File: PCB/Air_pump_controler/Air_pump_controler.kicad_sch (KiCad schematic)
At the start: 28 parts, among them J1 Conn_01x03_Pin, J2 USB IN, J4 Motor_conn, Q1 AP30N03DF, U1 CH32V003F4U6

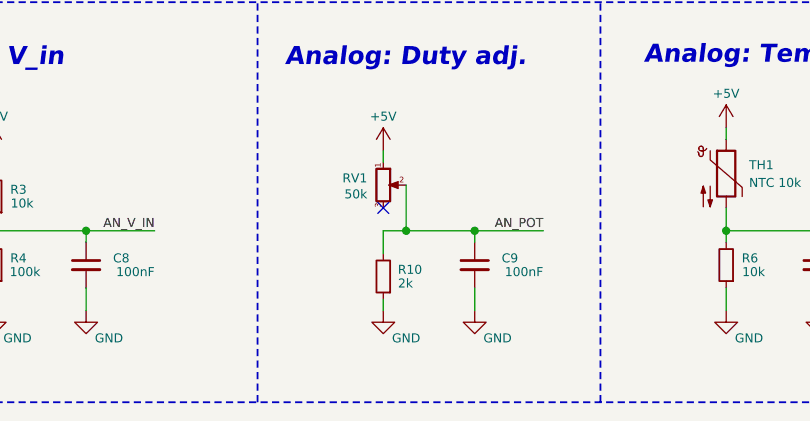
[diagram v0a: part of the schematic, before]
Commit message: Update
input voltage compensation for duty cycle
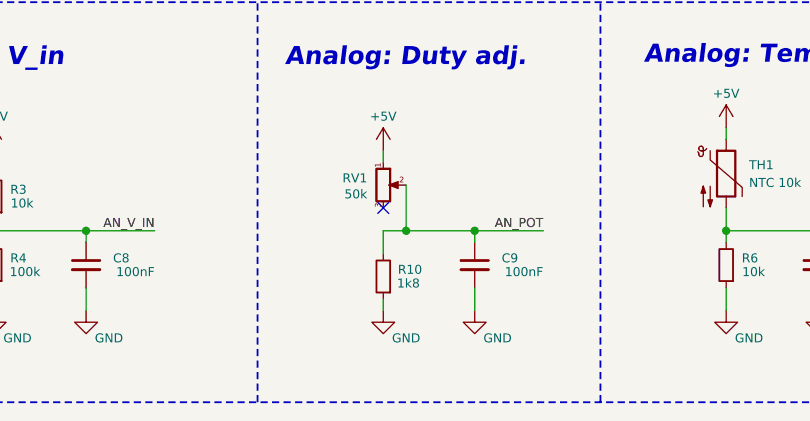
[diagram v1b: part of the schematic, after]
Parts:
- R10: value 2k -> 1k8
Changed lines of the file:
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@@
 			)
 		)
-		(property "Value" "2k"
-			(at 71.882 112.522 0)
+		(property "Value" "1k8"
+			(at 72.644 112.522 0)
 			(effects
 				(font

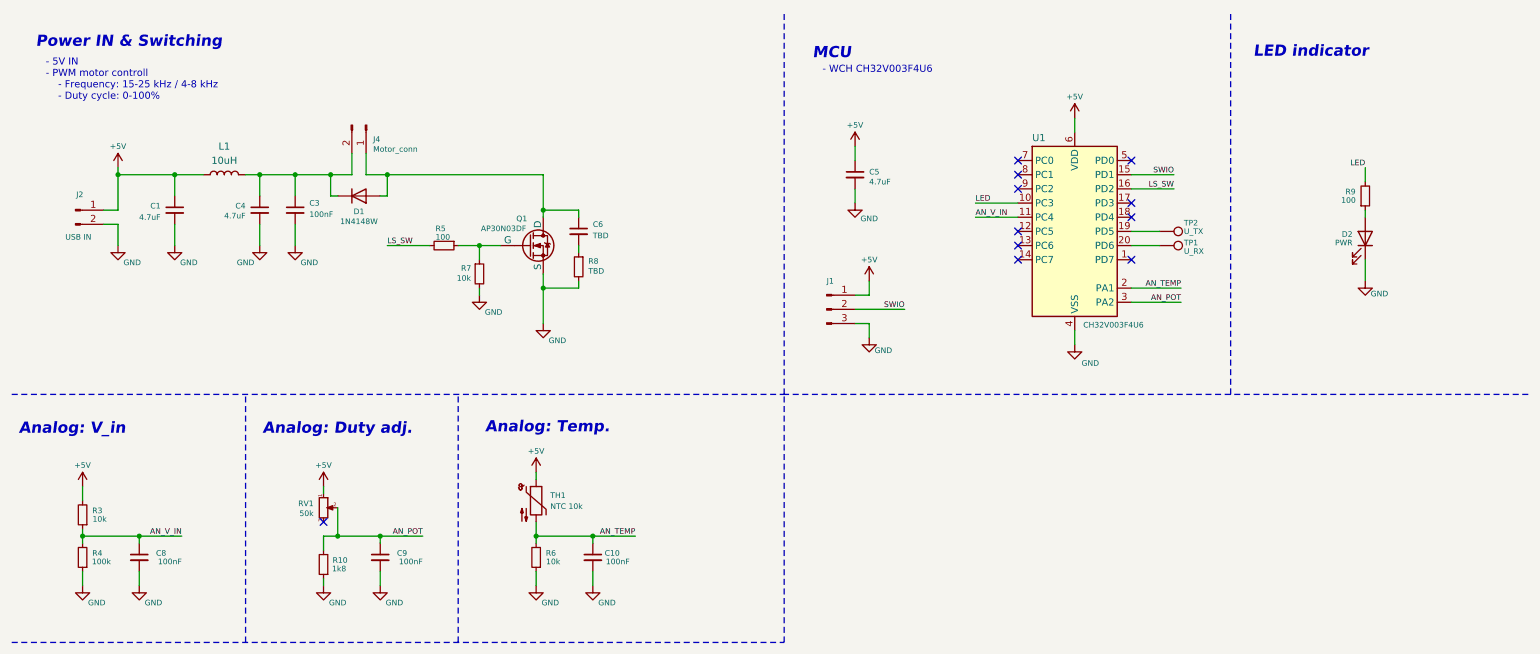
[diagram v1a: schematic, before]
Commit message: Update
changed potenciometer voltage divider, added filter cap
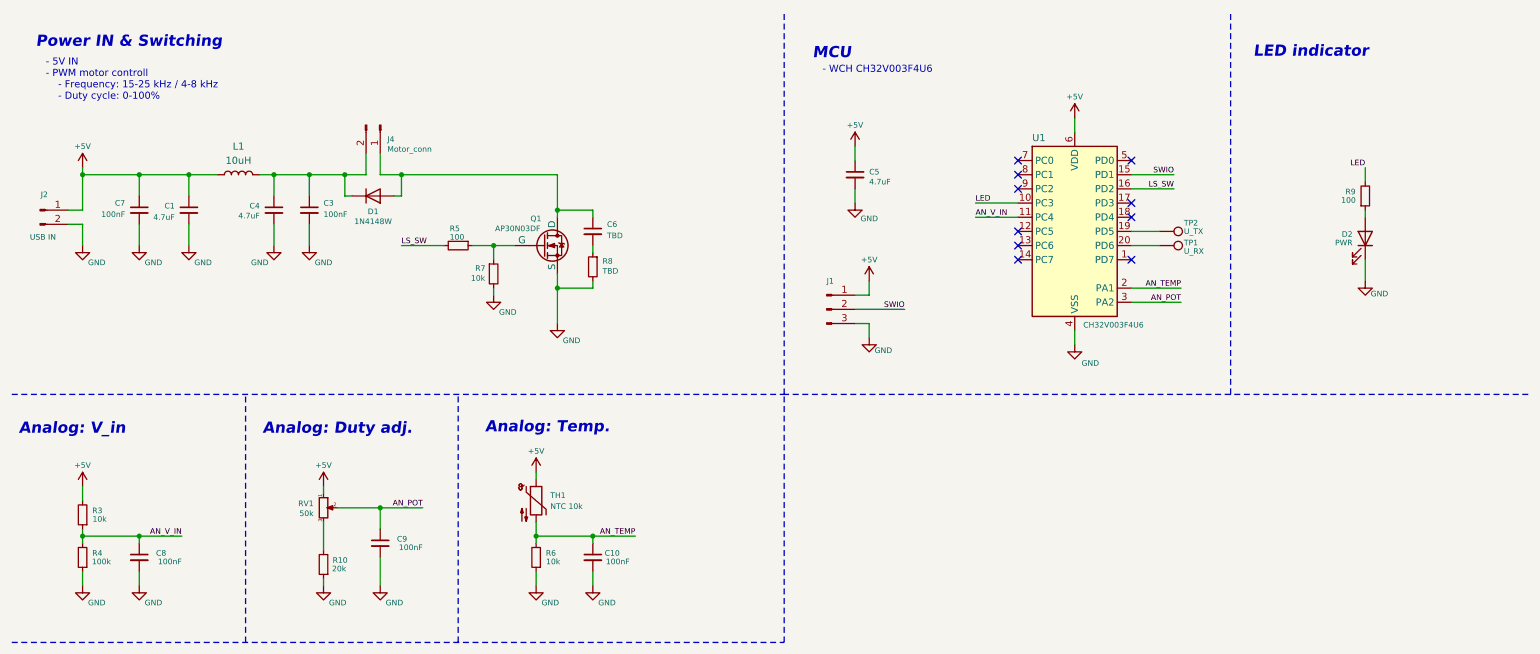
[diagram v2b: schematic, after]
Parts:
- added C7: 100nF, Capacitor_SMD:C_0603_1608Metric, symbol Device:C_Small
- R10: value 1k8 -> 20k
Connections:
- net +5V: now also C7.1
- net AN_POT: no longer R10.2
- net GND: now also C7.2
- net at RV1.3: now also R10.2
- no-connect marks 11 -> 10
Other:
- moved on the sheet: C1, C3, C4, C6, C9, D1, J2, J4, L1, Q1, R5, R7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

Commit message: Update
added filter cap on input
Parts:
- removed C7: 100nF, Capacitor_SMD:C_0603_1608Metric, symbol Device:C_Small
- added C11, C12: 10nF, Capacitor_SMD:C_0402_1005Metric, symbol Device:C_Small
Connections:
- net +5V: now also C11.1, C12.1
- net GND: now also C11.2, C12.2
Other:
- moved on the sheet: C1, C3, C4, C6, D1, J4, L1, Q1, R5, R7, R8

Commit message: Update
added filter cap on input
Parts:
- added C13: 10nF, Capacitor_SMD:C_0402_1005Metric, symbol Device:C_Small
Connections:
- net +5V: now also C13.1
- net GND: now also C13.2
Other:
- moved on the sheet: C5
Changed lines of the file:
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@@
 	)
 	(junction
+		(at 167.64 38.1)
+		(diameter 0)
+		(color 0 0 0 0)
+	)
+	(junction
 		(at 74.93 41.91)
 		(diameter 0)
@@
 	(wire
 		(pts
-			(xy 163.83 44.45) (xy 163.83 46.99)
+			(xy 167.64 44.45) (xy 167.64 46.99)
 		)
 		(stroke
@@
 	(wire
 		(pts
+			(xy 162.56 39.37) (xy 162.56 38.1)
+		)
+		(stroke
+			(width 0)
+			(type default)
+		)
+	)
+	(wire
+		(pts
 			(xy 102.87 45.72) (xy 104.14 45.72)
 		)
@@
 	(wire
 		(pts
+			(xy 162.56 44.45) (xy 162.56 46.99)
+		)
+		(stroke
+			(width 0)
+			(type default)
+		)
+	)
+	(wire
+		(pts
 			(xy 93.98 45.72) (xy 93.98 41.91)
 		)
@@
 	(wire
 		(pts
-			(xy 163.83 36.83) (xy 163.83 39.37)
+			(xy 167.64 36.83) (xy 167.64 38.1)
 		)
 		(stroke
@@
 	(wire
 		(pts
+			(xy 162.56 38.1) (xy 167.64 38.1)
+		)
+		(stroke
+			(width 0)
+			(type default)
+		)
+	)
+	(wire
+		(pts
 			(xy 35.56 50.8) (xy 35.56 54.61)
 		)
@@
 	(wire
 		(pts
+			(xy 167.64 38.1) (xy 167.64 39.37)
+		)
+		(stroke
+			(width 0)
+			(type default)
+		)
+	)
+	(wire
+		(pts
 			(xy 35.56 113.03) (xy 35.56 115.57)
 		)
@@
 	)
 	(symbol
+		(lib_id "Device:C_Small")
+		(at 162.56 41.91 0)
+		(mirror y)
+		(unit 1)
+		(exclude_from_sim no)
+		(in_bom yes)
+		(on_board yes)
+		(dnp no)
+		(property "Reference" "C13"
+			(at 160.02 41.402 0)
+			(effects
+				(font
+					(size 1 1)
+				)
+				(justify left)
+			)
+		)
+		(property "Value" "10nF"
+			(at 160.02 43.1863 0)
+			(effects
+				(font
+					(size 1 1)
+				)
+				(justify left)
+			)
+		)
+		(property "Footprint" "Capacitor_SMD:C_0402_1005Metric"
+			(at 162.56 41.91 0)
+			(effects
+				(font
+					(size 1.27 1.27)
+				)
+				(hide yes)
+			)
+		)
+		(property "Datasheet" "~"
+			(at 162.56 41.91 0)
+			(effects
+				(font
+					(size 1.27 1.27)
+				)
+				(hide yes)
+			)
+		)
+		(property "Description" "Unpolarized capacitor, small symbol"
+			(at 162.56 41.91 0)
+			(effects
+				(font
+					(size 1.27 1.27)
+				)
+				(hide yes)
+			)
+		)
+		(pin "1"
+		)
+		(pin "2"
+		)
+		(instances
+			(project "Air_pump_controler"
+				(path "/3c68f82e-901f-404a-869f-4b45aa33f8e4"
+					(reference "C13")
+					(unit 1)
+				)
+			)
+		)
+	)
+	(symbol
 		(lib_id "power:GND")
-		(at 163.83 46.99 0)
+		(at 167.64 46.99 0)
 		(unit 1)
 		(exclude_from_sim no)
@@
 		(dnp no)
 		(property "Reference" "#PWR04"
-			(at 163.83 53.34 0)
+			(at 167.64 53.34 0)
 			(effects
 				(font
@@
 		)
 		(property "Value" "GND"
-			(at 166.37 49.784 0)
+			(at 170.18 49.784 0)
 			(effects
 				(font
@@
 		)
 		(property "Footprint" ""
-			(at 163.83 46.99 0)
+			(at 167.64 46.99 0)
 			(effects
 				(font
@@
 		)
 		(property "Datasheet" ""
-			(at 163.83 46.99 0)
+			(at 167.64 46.99 0)
 			(effects
 				(font
@@
 		)
 		(property "Description" "Power symbol creates a global label with name \"GND\" , ground"
-			(at 163.83 46.99 0)
+			(at 167.64 46.99 0)
 			(effects
 				(font
@@
 	(symbol
 		(lib_id "power:GND")
+		(at 162.56 46.99 0)
+		(mirror y)
+		(unit 1)
+		(exclude_from_sim no)
+		(in_bom yes)
+		(on_board yes)
+		(dnp no)
+		(property "Reference" "#PWR025"
+			(at 162.56 53.34 0)
+			(effects
+				(font
+					(size 1.27 1.27)
+				)
+				(hide yes)
+			)
+		)
+		(property "Value" "GND"
+			(at 160.02 50.038 0)
+			(effects
+				(font
+					(size 1 1)
+				)
+			)
+		)
+		(property "Footprint" ""
+			(at 162.56 46.99 0)
+			(effects
+				(font
+					(size 1.27 1.27)
+				)
+				(hide yes)
+			)
+		)
+		(property "Datasheet" ""
+			(at 162.56 46.99 0)
+			(effects
+				(font
+					(size 1.27 1.27)
+				)
+				(hide yes)
+			)
+		)
+		(property "Description" "Power symbol creates a global label with name \"GND\" , ground"
+			(at 162.56 46.99 0)
+			(effects
+				(font
+					(size 1.27 1.27)
+				)
+				(hide yes)
+			)
+		)
+		(pin "1"
+		)
+		(instances
+			(project "Air_pump_controler"
+				(path "/3c68f82e-901f-404a-869f-4b45aa33f8e4"
+					(reference "#PWR025")
+					(unit 1)
+				)
+			)
+		)
+	)
+	(symbol
+		(lib_id "power:GND")
 		(at 118.11 63.5 0)
 		(unit 1)
@@
 	(symbol
 		(lib_id "Device:C_Small")
-		(at 163.83 41.91 0)
+		(at 167.64 41.91 0)
 		(unit 1)
 		(exclude_from_sim no)
@@
 		(dnp no)
 		(property "Reference" "C5"
-			(at 166.37 41.402 0)
+			(at 170.18 41.402 0)
 			(effects
 				(font
@@
 		)
 		(property "Value" "4.7uF"
-			(at 166.37 43.1863 0)
+			(at 170.18 43.1863 0)
 			(effects
 				(font
@@
 		)
 		(property "Footprint" "Capacitor_SMD:C_0402_1005Metric"
-			(at 163.83 41.91 0)
+			(at 167.64 41.91 0)
 			(effects
 				(font
@@
 		)
 		(property "Datasheet" "~"
-			(at 163.83 41.91 0)
+			(at 167.64 41.91 0)
 			(effects
 				(font
@@
 		)
 		(property "Description" "Unpolarized capacitor, small symbol"
-			(at 163.83 41.91 0)
+			(at 167.64 41.91 0)
 			(effects
 				(font
@@
 	(symbol
 		(lib_id "power:+5V")
-		(at 163.83 36.83 0)
+		(at 167.64 36.83 0)
 		(unit 1)
 		(exclude_from_sim no)
@@
 		(dnp no)
 		(property "Reference" "#PWR03"
-			(at 163.83 40.64 0)
+			(at 167.64 40.64 0)
 			(effects
 				(font
@@
 		)
 		(property "Value" "+5V"
-			(at 163.83 33.02 0)
+			(at 167.64 33.02 0)
 			(effects
 				(font
@@
 		)
 		(property "Footprint" ""
-			(at 163.83 36.83 0)
+			(at 167.64 36.83 0)
 			(effects
 				(font
@@
 		)
 		(property "Datasheet" ""
-			(at 163.83 36.83 0)
+			(at 167.64 36.83 0)
 			(effects
 				(font
@@
 		)
 		(property "Description" "Power symbol creates a global label with name \"+5V\""
-			(at 163.83 36.83 0)
+			(at 167.64 36.83 0)
 			(effects
 				(font
